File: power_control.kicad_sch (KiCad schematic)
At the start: 6 parts, among them U2 INA228, U3 INA228, U4 INA228

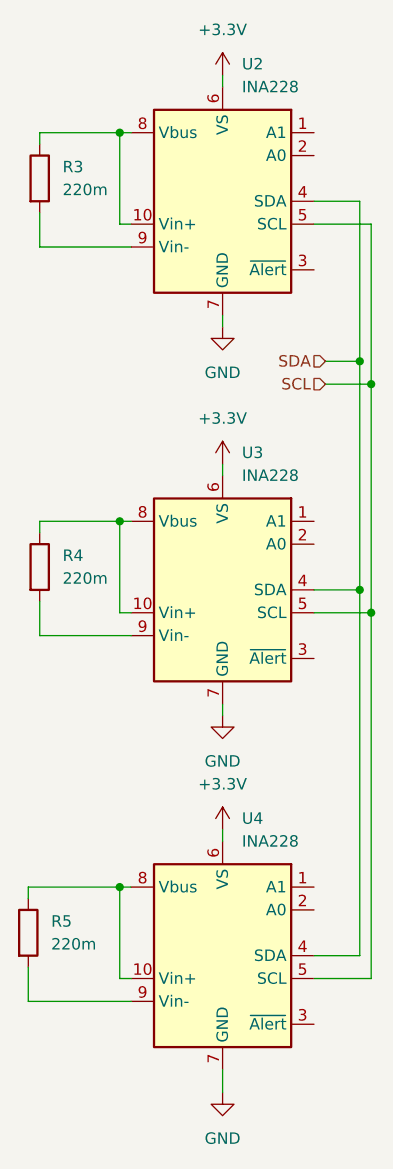
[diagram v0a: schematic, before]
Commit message: Most Components added, added USB subsystem
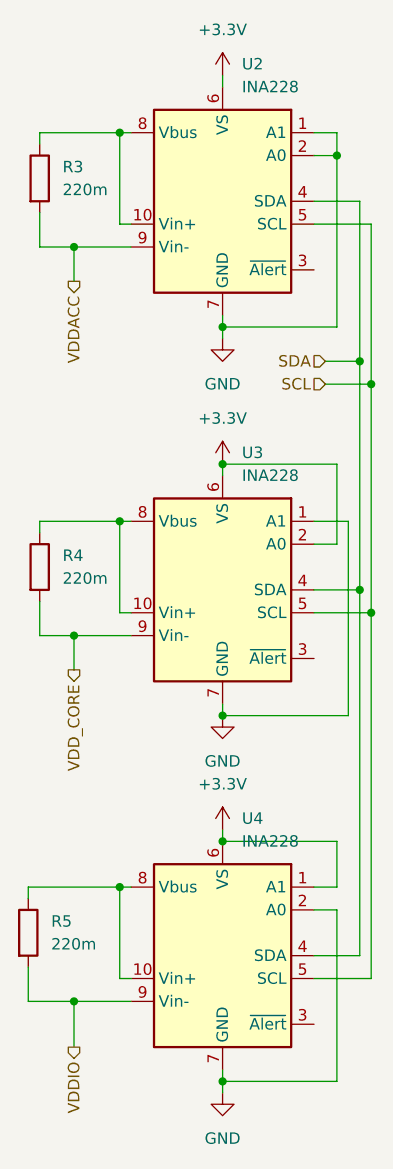
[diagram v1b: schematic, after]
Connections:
- net +3.3V: now also U3.2 (A0), U4.1 (A1)
- net GND: now also U2.1 (A1), U2.2 (A0), U3.1 (A1), U4.2 (A0)
- net VDD_CORE: now reaches R4.2, U3.9 (Vin-)
- net VDDACC: now reaches R3.2, U2.9 (Vin-)
- net VDDIO: now reaches R5.2, U4.9 (Vin-)

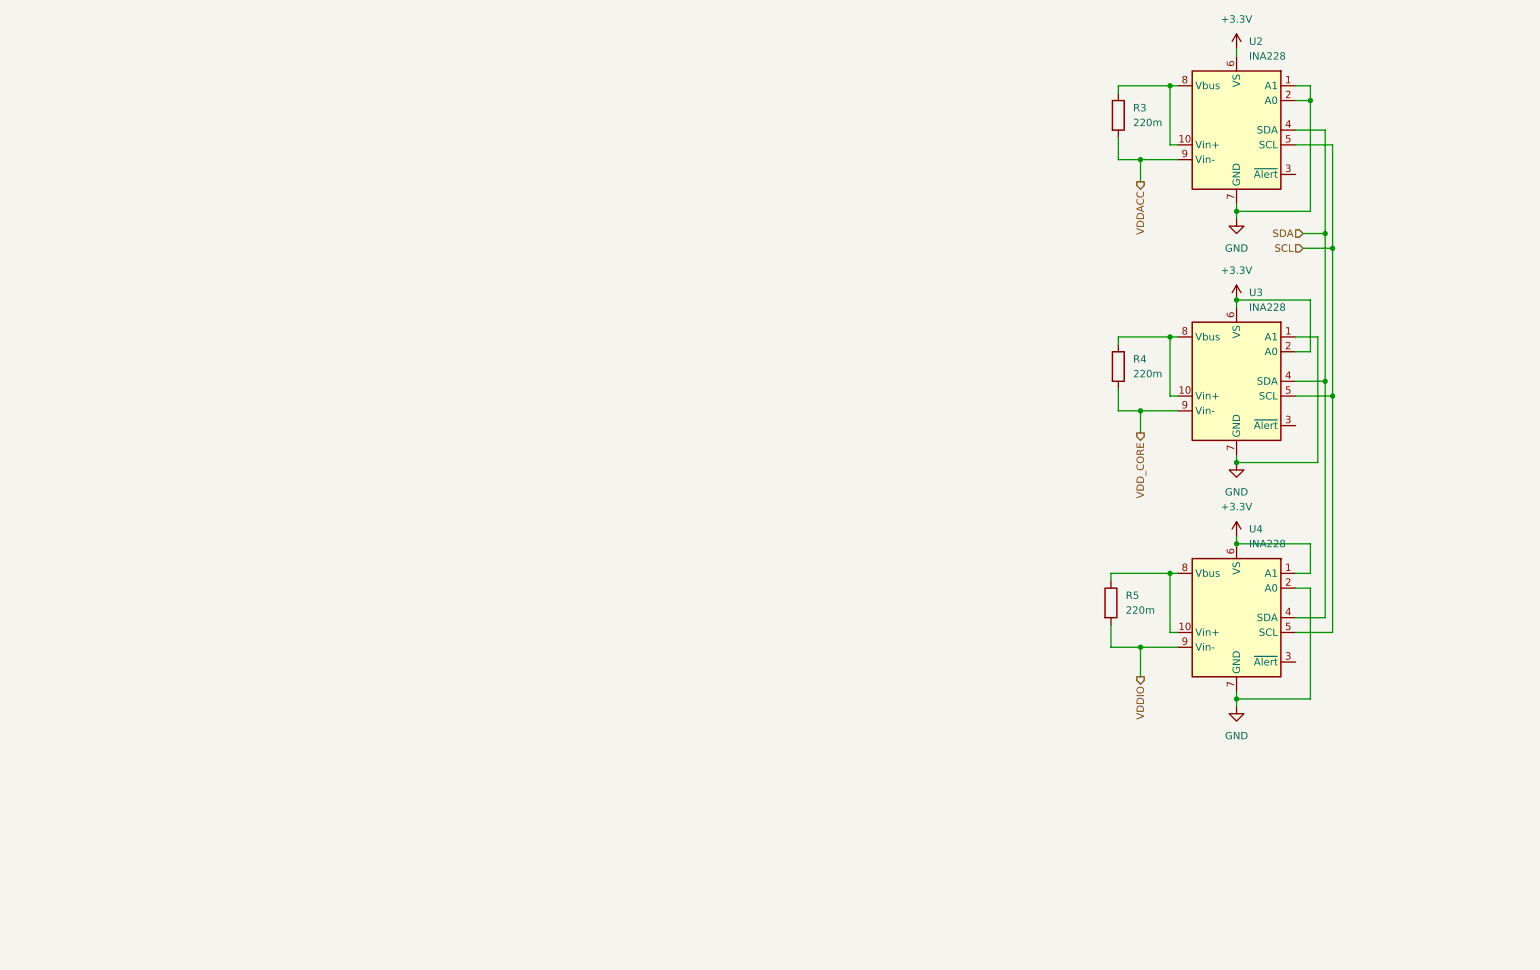
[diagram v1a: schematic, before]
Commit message: Major components all added to schematics. Added document info for FPGA pins
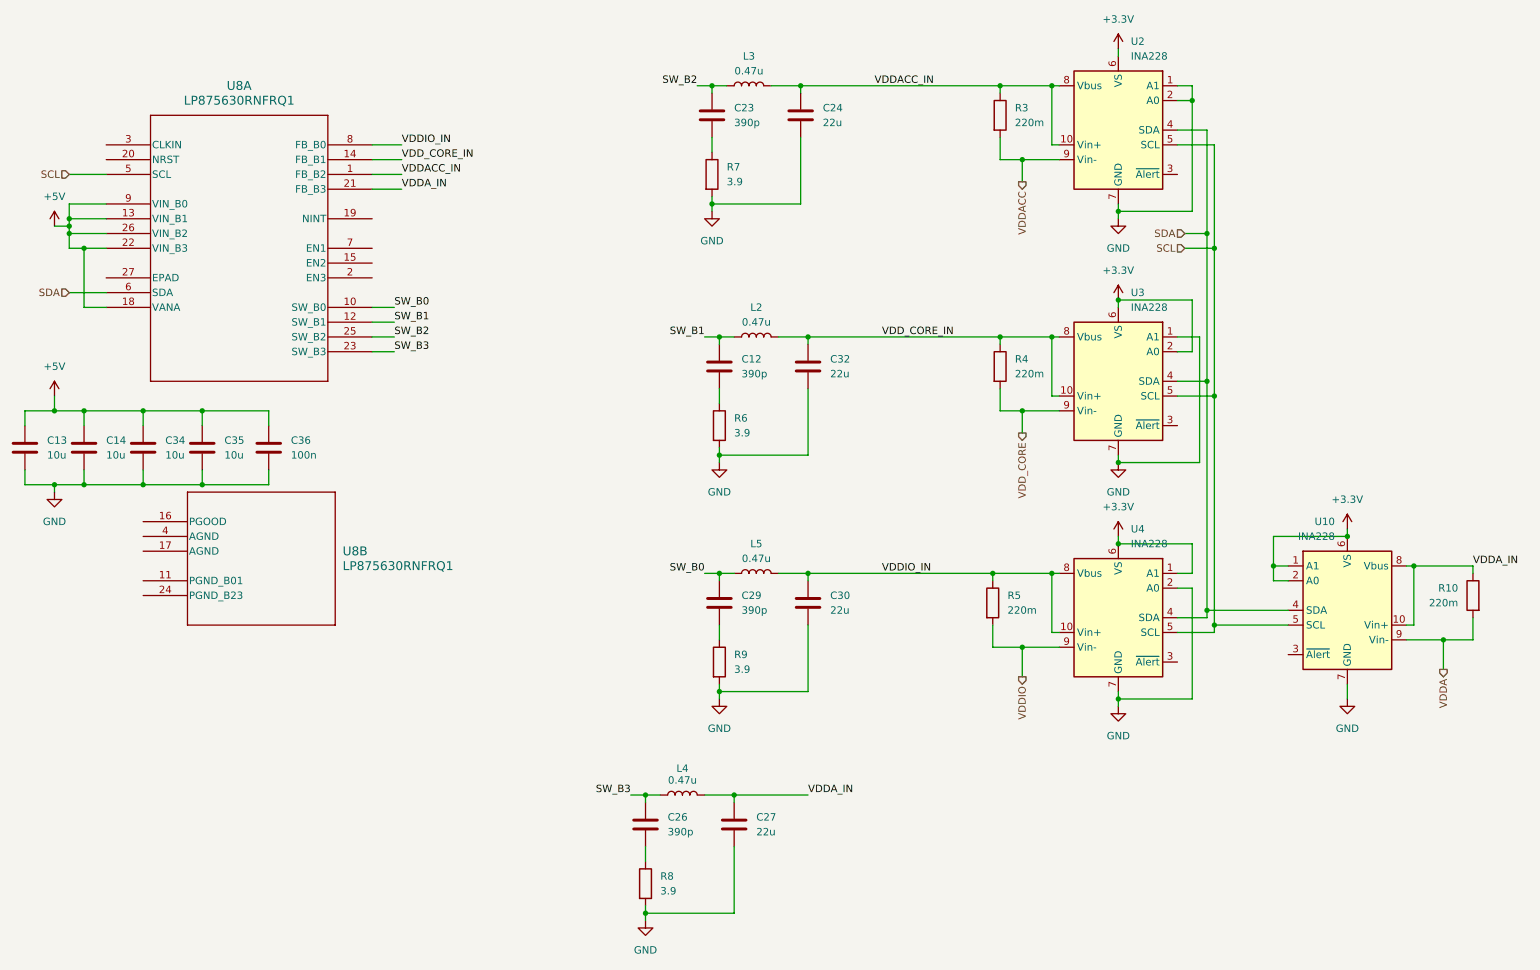
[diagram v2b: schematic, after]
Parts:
- added C12, C23, C26, C29: 390p, Capacitor_SMD:C_0402_1005Metric, symbol Device:C
- added C13, C14, C34, C35: 10u, Capacitor_SMD:C_0805_2012Metric, symbol Device:C
- added C24, C27, C30, C32: 22u, Capacitor_SMD:C_1206_3216Metric, symbol Device:C
- added C36: 100n, Capacitor_SMD:C_0402_1005Metric, symbol Device:C
- added L2, L3, L4, L5: 0.47u, Inductor_SMD:L_1008_2520Metric, symbol Device:L
- added R10: 220m, Resistor_SMD:R_2010_5025Metric, symbol Device:R
- added R6, R7, R8, R9: 3.9, Resistor_SMD:R_0402_1005Metric, symbol Device:R
- added U10: INA228, Package_SO:VSSOP-10_3x3mm_P0.5mm, symbol Sensor_Energy:INA228
- added U8: LP875630RNFRQ1, RNF26_TEX, symbol LP87563-Q1:LP875630RNFRQ1
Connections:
- net +3.3V: now also U10.1 (A1), U10.2 (A0), U10.6 (VS)
- net GND: now also C13.2, C14.2, C24.2, C27.2, C30.2, C32.2, C34.2, C35.2, C36.2, R6.2, R7.2, R8.2, R9.2, U10.7 (GND)
- net SCL: now also U10.5 (SCL), U8.5 (SCL)
- net SDA: now also U10.4 (SDA), U8.6 (SDA)
- net VDD_CORE_IN: now reaches R4.1, U3.10 (Vin+), U3.8 (Vbus)
- net VDD_CORE_IN: now also C32.1, L2.2, U8.14 (FB_B1)
- net VDDACC_IN: now reaches R3.1, U2.10 (Vin+), U2.8 (Vbus)
- net VDDACC_IN: now also C24.1, L3.2, U8.1 (FB_B2)
- net VDDIO_IN: now reaches R5.1, U4.10 (Vin+), U4.8 (Vbus)
- net VDDIO_IN: now also C30.1, L5.2, U8.8 (FB_B0)
- new net: C12.2, R6.1
- new net: C23.2, R7.1
- new net: C29.2, R9.1
- new net: C26.2, R8.1
- new net +5V: C13.1, C14.1, C34.1, C35.1, C36.1, U8.13 (VIN_B1), U8.18 (VANA), U8.22 (VIN_B3), U8.26 (VIN_B2), U8.9 (VIN_B0)
- new net SW_B0: C29.1, L5.1, U8.10 (SW_B0)
- new net SW_B1: C12.1, L2.1, U8.12 (SW_B1)
- new net SW_B2: C23.1, L3.1, U8.25 (SW_B2)
- new net SW_B3: C26.1, L4.1, U8.23 (SW_B3)
- new net VDDA: R10.2, U10.9 (Vin-)
- new net VDDA_IN: C27.1, L4.2, R10.1, U10.10 (Vin+), U10.8 (Vbus), U8.21 (FB_B3)
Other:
- moved on the sheet: R3, R4, R5, U2, U3, U4
